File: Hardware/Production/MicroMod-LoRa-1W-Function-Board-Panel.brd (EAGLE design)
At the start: 167.2 x 149.6 mm, 422 parts, among them J1 MICROMOD_STANDARD, J11 MICROMOD_STANDARD, J2 MICROMOD_STANDARD, J3 MICROMOD_STANDARD, J4 MICROMOD_STANDARD, J5 MICROMOD_STANDARD, J6 MICROMOD_STANDARD, J7 MICROMOD_STANDARD, Q1 20V/4.2A/52mΩ/1.4W, Q10 20V/4.2A/52mΩ/1.4W, Q11 5.8A/30V/35mΩ, Q12 5.8A/30V/35mΩ, Q13 20V/4.2A/52mΩ/1.4W, Q14 20V/4.2A/52mΩ/1.4W, Q15 5.8A/30V/35mΩ, Q16 5.8A/30V/35mΩ, Q17 20V/4.2A/52mΩ/1.4W, Q18 20V/4.2A/52mΩ/1.4W, Q19 5.8A/30V/35mΩ, Q2 20V/4.2A/52mΩ/1.4W, Q20 5.8A/30V/35mΩ, Q21 20V/4.2A/52mΩ/1.4W, Q22 20V/4.2A/52mΩ/1.4W, Q23 5.8A/30V/35mΩ, Q24 5.8A/30V/35mΩ, Q25 20V/4.2A/52mΩ/1.4W, Q26 20V/4.2A/52mΩ/1.4W, Q27 5.8A/30V/35mΩ, Q28 5.8A/30V/35mΩ, Q29 20V/4.2A/52mΩ/1.4W, Q3 20V/4.2A/52mΩ/1.4W, Q30 20V/4.2A/52mΩ/1.4W, Q31 5.8A/30V/35mΩ, Q32 5.8A/30V/35mΩ, Q4 5.8A/30V/35mΩ, Q5 5.8A/30V/35mΩ, Q6 20V/4.2A/52mΩ/1.4W, Q7 20V/4.2A/52mΩ/1.4W, Q8 5.8A/30V/35mΩ, Q9 5.8A/30V/35mΩ, U1 EEPROM, U10 EEPROM, U11 E19-915M30S, U12 EEPROM, U13 E19-915M30S, U14 EEPROM, U15 E19-915M30S, U16 EEPROM, U2 E19-915M30S, U3 EEPROM, U4 E19-915M30S, U5 E19-915M30S, U6 EEPROM, U7 E19-915M30S, U8 EEPROM, U9 E19-915M30S

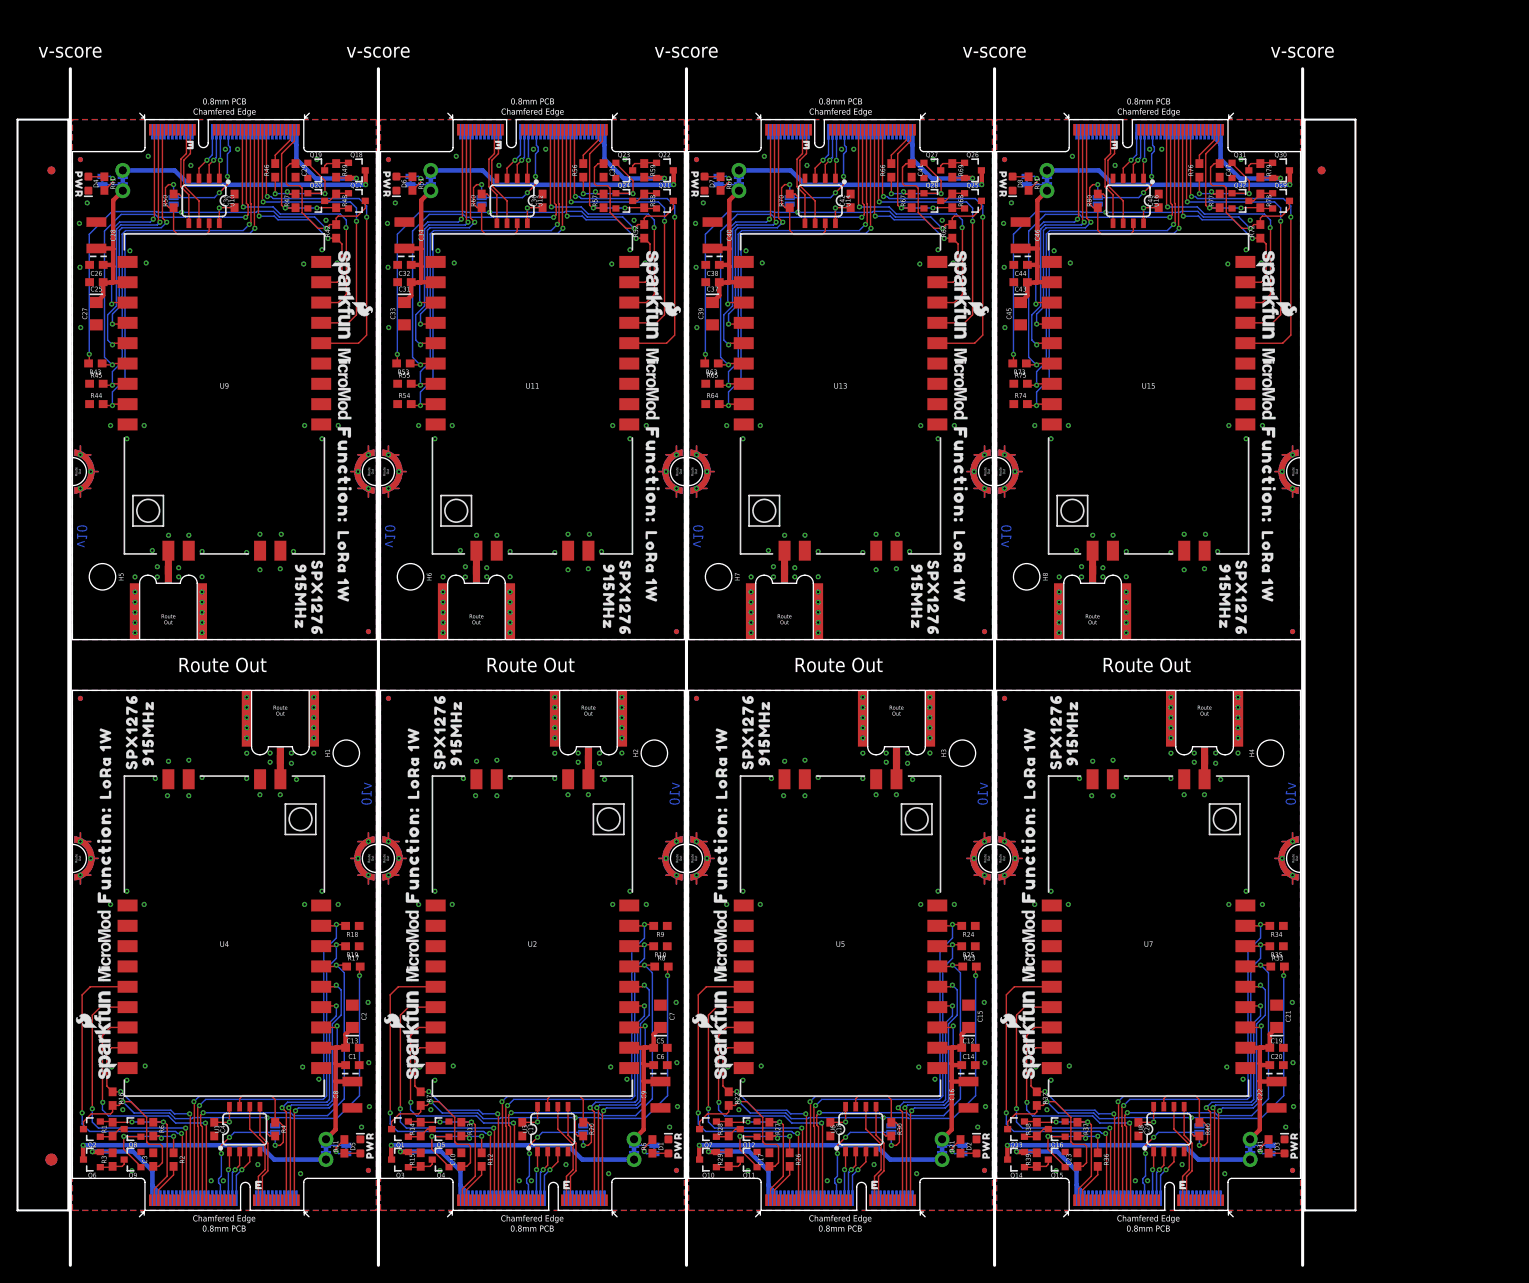
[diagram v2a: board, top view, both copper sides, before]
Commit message: Add SMA center pin. Increase panel gap to facilitate center pin. PCB is still v10.
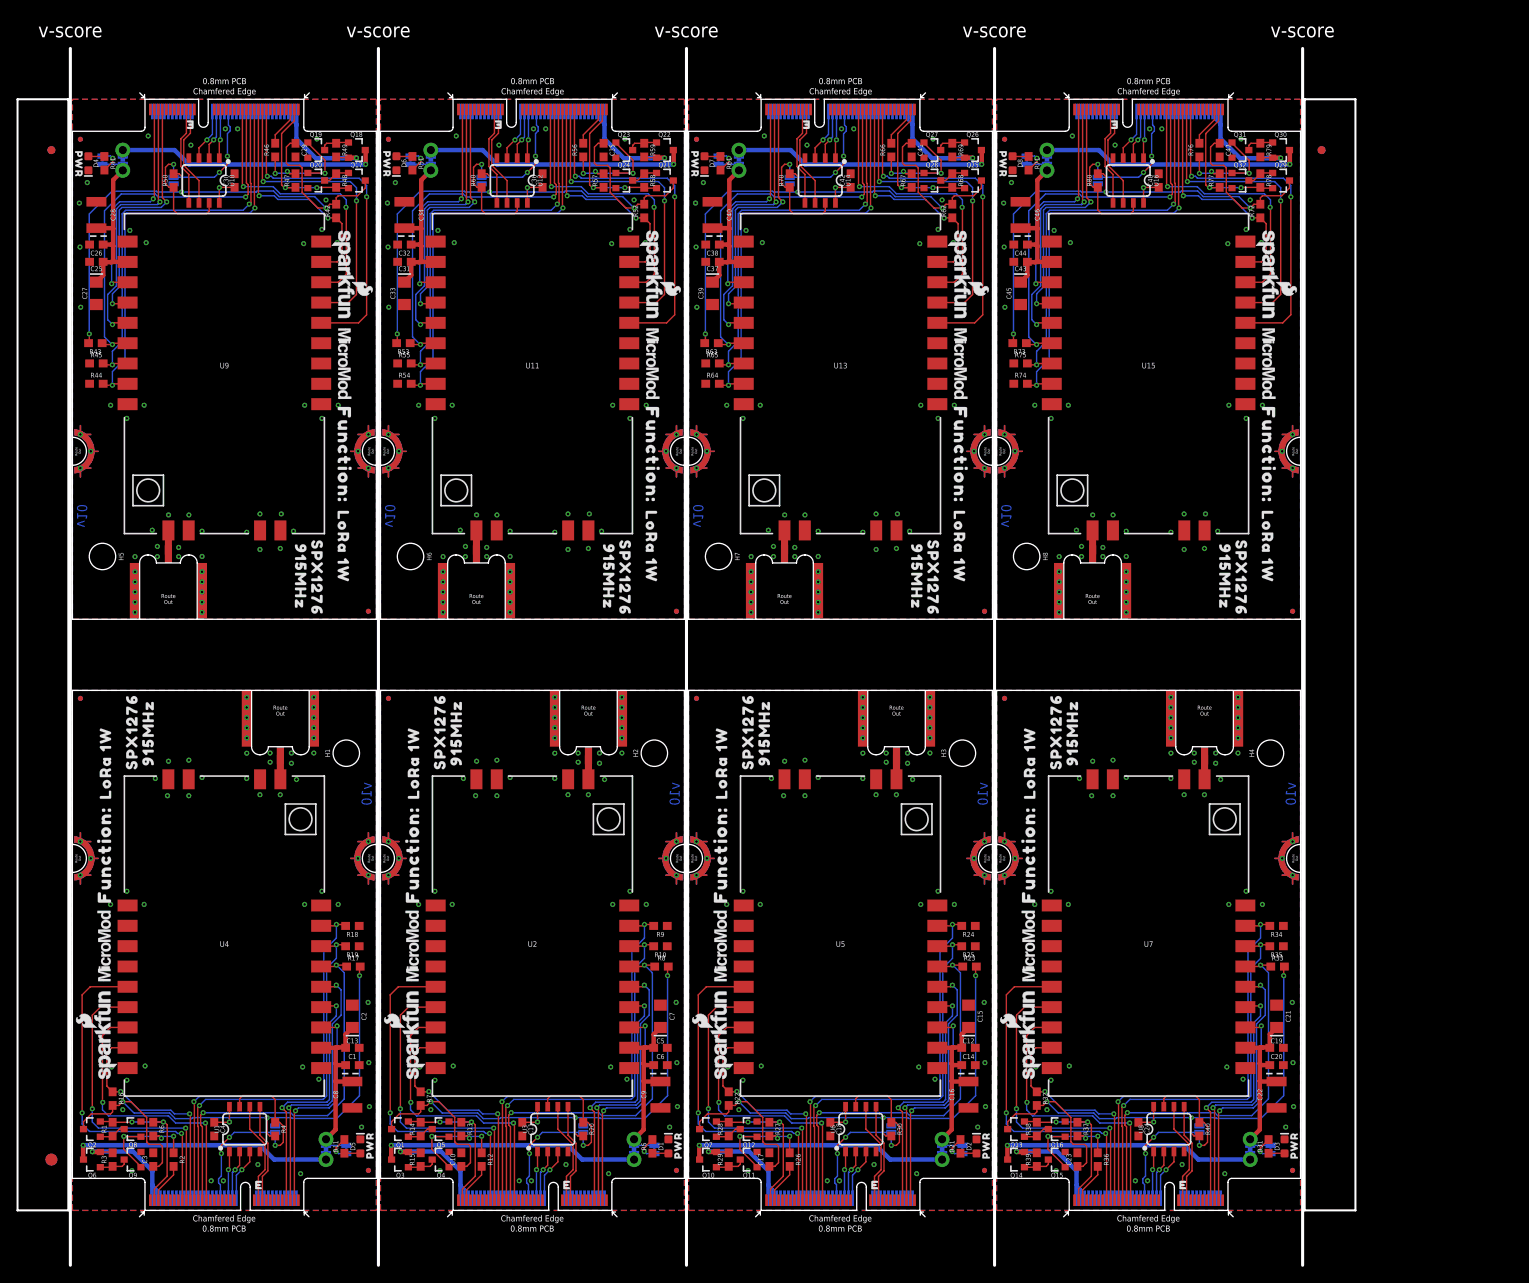
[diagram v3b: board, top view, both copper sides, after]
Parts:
- JP1, JP2, JP3, JP4, JP5, JP6, JP7, JP8: value (none) -> JUMPER-SMT_2_NO_SILK
- MEAS, MEAS1, MEAS2, MEAS3, MEAS4, MEAS5, MEAS6, MEAS7: value (none) -> JUMPER-COMBO_2_NC_TRACE
- PWR_LED, PWR_LED1, PWR_LED2, PWR_LED3, PWR_LED4, PWR_LED5, PWR_LED6, PWR_LED7: value (none) -> JUMPER-SMT_2_NC_TRACE_SILK
- moved C29 2.54 mm to (27.9, 132.5)
- moved C35 2.54 mm to (66.4, 132.5)
- moved C41 2.54 mm to (104.9, 132.5)
- moved C47 2.54 mm to (143.4, 132.5)
- moved E$1 2.54 mm to (-2.62, 132.5)
- moved E$2 2.54 mm to (-2.62, 132.5)
- moved E$3 2.54 mm to (156.1, 132.5)
- moved E$4 2.54 mm to (156.1, 132.5)
- moved Q18 2.54 mm to (35.5, 132.5)
- moved Q19 2.54 mm to (30.4, 132.5)
- moved Q22 2.54 mm to (74.0, 132.5)
- moved Q23 2.54 mm to (68.9, 132.5)
- moved Q26 2.54 mm to (112.5, 132.5)
- moved Q27 2.54 mm to (107.4, 132.5)
- moved Q30 2.54 mm to (151.0, 132.5)
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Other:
- board size 167.2 x 149.6 mm -> 167.2 x 152.1 mm
- board text removed: "Route Out"
